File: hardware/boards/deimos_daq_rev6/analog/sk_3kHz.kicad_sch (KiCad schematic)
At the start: 9 parts, among them U17001 OPA196xDBV

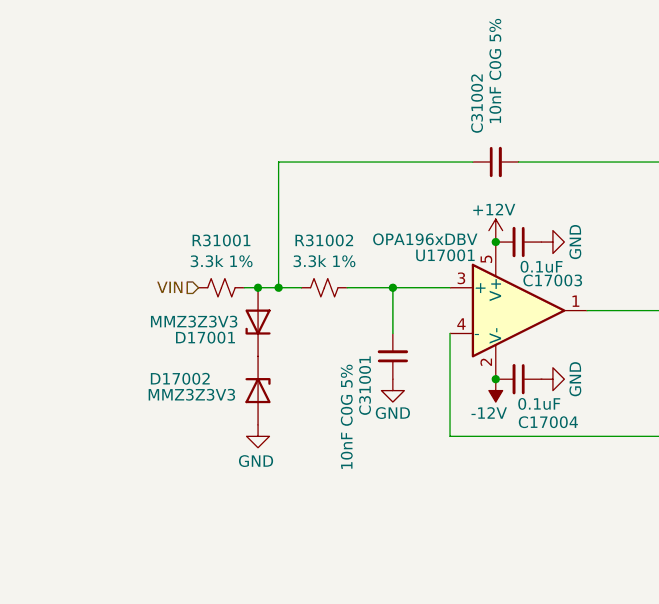
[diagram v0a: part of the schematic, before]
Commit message: move clamp diodes in schematic for filters. Add pulldown on ktype amp.
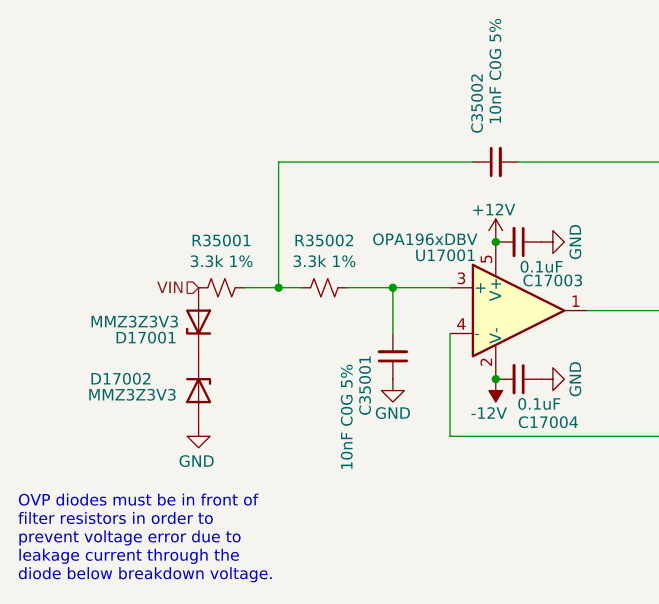
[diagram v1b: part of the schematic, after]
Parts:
- renumbered C31001 to C35001, C31002 to C35002, R31001 to R35001, R31002 to R35002
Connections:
- net VIN: now also D17001.2 (A)
- net at C35002.1, R35001.2, R35002.1: no longer D17001.2 (A)
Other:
- note added: "OVP diodes must be in front of filter resistors in order to prevent voltage error due to leakage current through the diode below breakdown voltage."
- moved on the sheet: D17001, D17002
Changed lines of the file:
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@@
-	)
-	(junction
-		(at 86.614 82.55)
-		(diameter 0)
-		(color 0 0 0 0)
 	)
 	(junction
@@
 	(wire
 		(pts
-			(xy 85.09 82.55) (xy 86.614 82.55)
+			(xy 85.09 82.55) (xy 88.9 82.55)
 		)
 		(stroke
@@
 	(wire
 		(pts
-			(xy 86.614 82.55) (xy 88.9 82.55)
+			(xy 107.95 99.06) (xy 133.35 99.06)
 		)
 		(stroke
@@
 	(wire
 		(pts
-			(xy 107.95 99.06) (xy 133.35 99.06)
+			(xy 101.6 82.55) (xy 107.95 82.55)
 		)
 		(stroke
@@
 	(wire
 		(pts
-			(xy 101.6 82.55) (xy 107.95 82.55)
+			(xy 88.9 68.58) (xy 88.9 82.55)
 		)
 		(stroke
@@
 	(wire
 		(pts
-			(xy 88.9 68.58) (xy 88.9 82.55)
+			(xy 110.49 68.58) (xy 88.9 68.58)
 		)
 		(stroke
@@
 	(wire
 		(pts
-			(xy 110.49 68.58) (xy 88.9 68.58)
+			(xy 133.35 99.06) (xy 133.35 85.09)
 		)
 		(stroke
@@
 		)
 	)
-	(wire
-		(pts
-			(xy 133.35 99.06) (xy 133.35 85.09)
-		)
-		(stroke
-			(width 0)
-			(type default)
+	(text "OVP diodes must be in front of\nfilter resistors in order to\nprevent voltage error due to\nleakage current through the\ndiode below breakdown voltage."
+		(exclude_from_sim no)
+		(at 59.944 110.49 0)
+		(effects
+			(font
+				(size 1.27 1.27)
+			)
+			(justify left)
 		)
 	)
@@
 		(on_board yes)
 		(dnp no)
-		(property "Reference" "C31001"
+		(property "Reference" "C35001"
 			(at 98.552 96.774 90)
 			(effects
@@
 	(symbol
 		(lib_id "Device:D_Zener")
-		(at 86.614 93.98 270)
+		(at 80.01 93.98 270)
 		(unit 1)
 		(exclude_from_sim no)
@@
 		(dnp no)
 		(property "Reference" "D17002"
-			(at 77.978 92.71 90)
+			(at 71.374 92.71 90)
 			(effects
 				(font
@@
 		)
 		(property "Value" "MMZ3Z3V3"
-			(at 79.248 94.488 90)
+			(at 72.644 94.488 90)
 			(effects
 				(font
@@
 		)
 		(property "Footprint" "Diode_SMD:D_SOD-323"
-			(at 86.614 93.98 0)
+			(at 80.01 93.98 0)
 			(effects
 				(font
@@
 		)
 		(property "Datasheet" "~"
-			(at 86.614 93.98 0)
+			(at 80.01 93.98 0)
 			(effects
 				(font
@@
 		)
 		(property "Description" ""
-			(at 86.614 93.98 0)
+			(at 80.01 93.98 0)
 			(effects
 				(font
@@
 		)
 		(property "LCSC" "C52056"
-			(at 86.614 93.98 0)
+			(at 80.01 93.98 0)
 			(effects
 				(font
@@
 	(symbol
 		(lib_id "Device:D_Zener")
-		(at 86.614 86.36 90)
+		(at 80.01 86.36 90)
 		(unit 1)
 		(exclude_from_sim no)
@@
 		(dnp no)
 		(property "Reference" "D17001"
-			(at 80.772 88.138 90)
+			(at 74.168 88.138 90)
 			(effects
 				(font
@@
 		)
 		(property "Value" "MMZ3Z3V3"
-			(at 79.502 86.36 90)
+			(at 72.898 86.36 90)
 			(effects
 				(font
@@
 		)
 		(property "Footprint" "Diode_SMD:D_SOD-323"
-			(at 86.614 86.36 0)
+			(at 80.01 86.36 0)
 			(effects
 				(font
@@
 		)
 		(property "Datasheet" "~"
-			(at 86.614 86.36 0)
+			(at 80.01 86.36 0)
 			(effects
 				(font
@@
 		)
 		(property "Description" ""
-			(at 86.614 86.36 0)
+			(at 80.01 86.36 0)
 			(effects
 				(font
@@
 		)
 		(property "LCSC" "C52056"
-			(at 86.614 86.36 0)
+			(at 80.01 86.36 0)
 			(effects
 				(font
@@
 	(symbol
 		(lib_id "power:GND")
-		(at 86.614 97.79 0)
+		(at 80.01 97.79 0)
 		(unit 1)
 		(exclude_from_sim no)
@@
 		(dnp no)
 		(property "Reference" "#PWR17002"
-			(at 86.614 104.14 0)
+			(at 80.01 104.14 0)
 			(effects
 				(font
@@
 		)
 		(property "Value" "GND"
-			(at 88.392 101.854 0)
+			(at 81.788 101.854 0)
 			(effects
 				(font
@@
 		)
 		(property "Footprint" ""
-			(at 86.614 97.79 0)
+			(at 80.01 97.79 0)
 			(effects
 				(font
@@
 		)
 		(property "Datasheet" ""
-			(at 86.614 97.79 0)
+			(at 80.01 97.79 0)
 			(effects
 				(font
@@
 		)
 		(property "Description" ""
-			(at 86.614 97.79 0)
+			(at 80.01 97.79 0)
 			(effects
 				(font
@@
 		(on_board yes)
 		(dnp no)
-		(property "Reference" "R31001"
+		(property "Reference" "R35001"
 			(at 82.55 77.343 90)
 			(effects
@@
 		(on_board yes)
 		(dnp no)
-		(property "Reference" "R31002"
+		(property "Reference" "R35002"
 			(at 93.98 77.343 90)
 			(effects
@@
 		(on_board yes)
 		(dnp no)
-		(property "Reference" "C31002"
+		(property "Reference" "C35002"
 			(at 110.998 58.674 0)
 			(effects
@@
 		(on_board yes)
 		(dnp no)
-		(property "Reference" "#PWR195"
+		(property "Reference" "#PWR205"
 			(at 101.6 99.06 0)
 			(effects

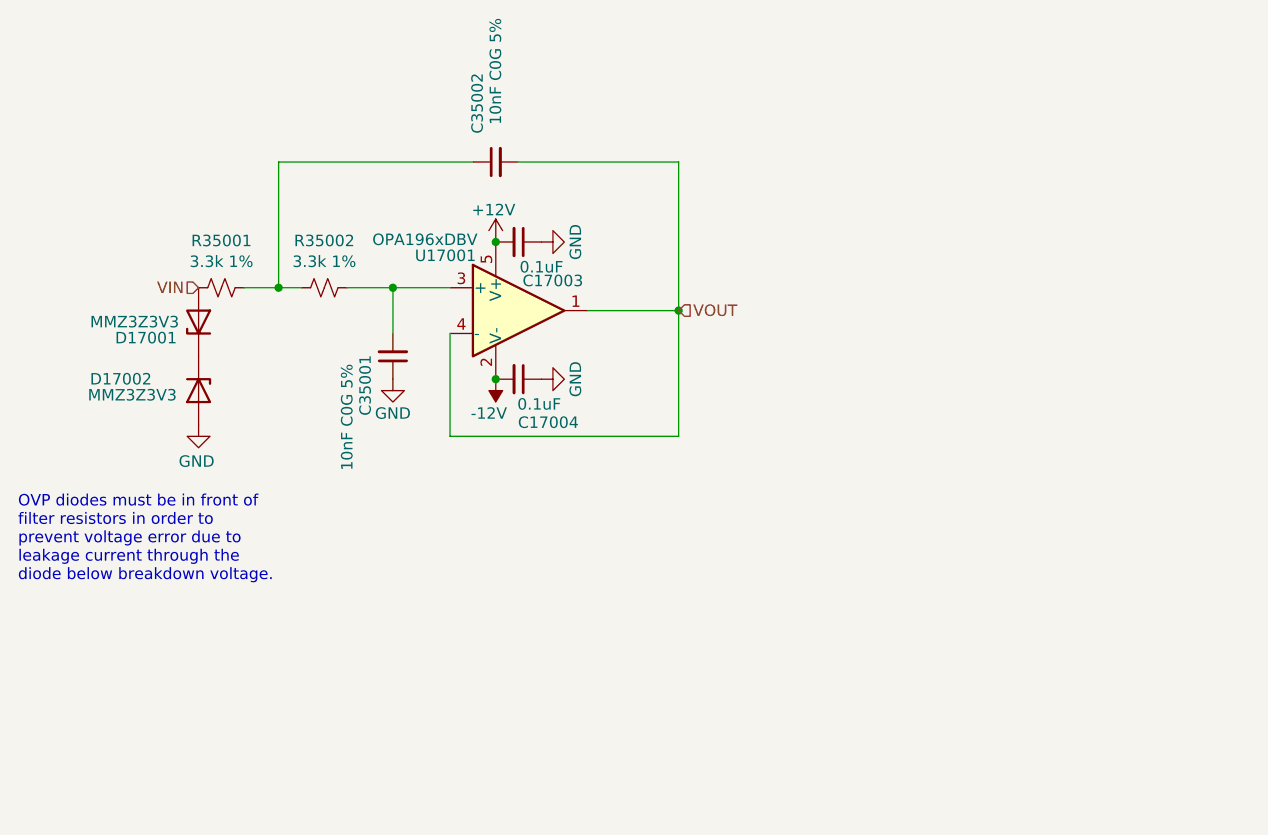
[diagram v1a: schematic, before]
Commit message: move ovp diodes behind filter amps. wip to implement 5V LDO.
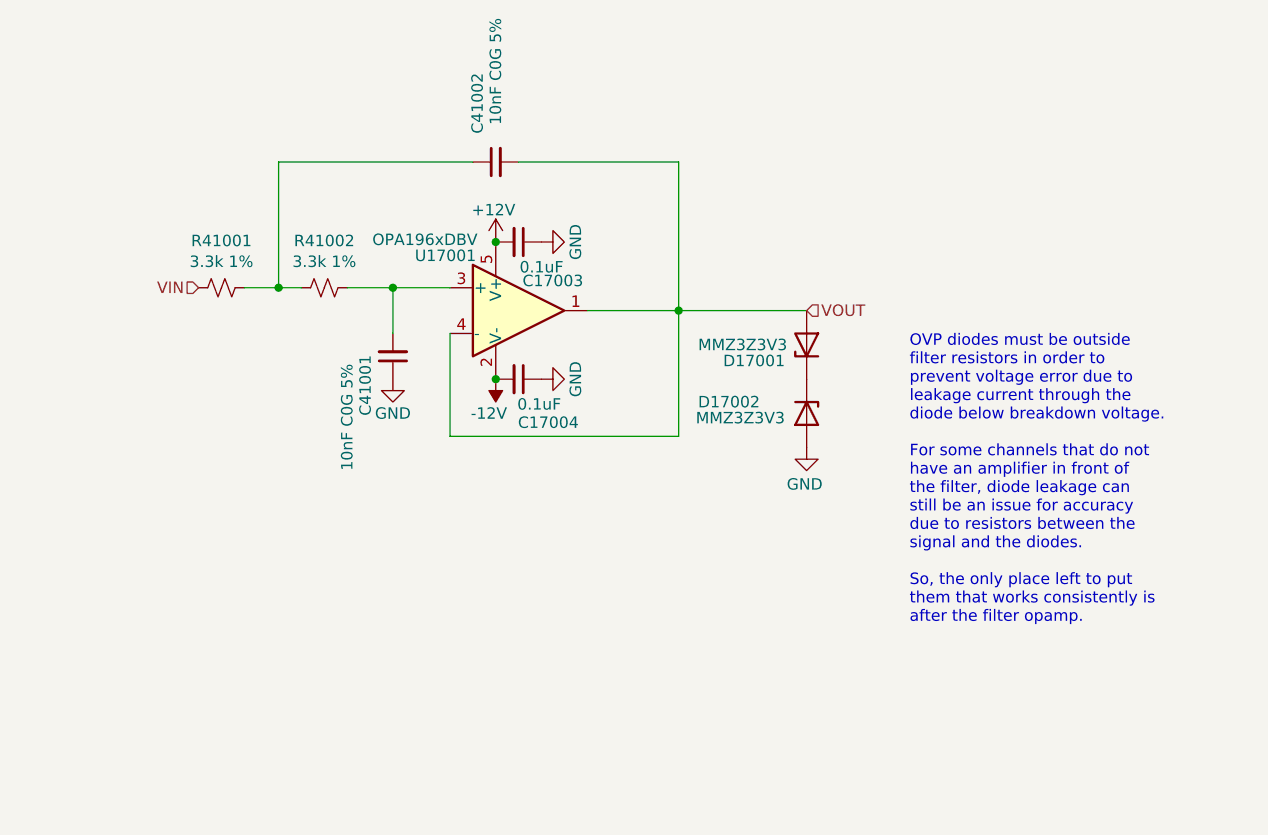
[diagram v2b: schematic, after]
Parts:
- renumbered C35001 to C41001, C35002 to C41002, R35001 to R41001, R35002 to R41002
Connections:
- net VIN: no longer D17001.2 (A)
- net VOUT: now also D17001.2 (A)
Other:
- note added: "OVP diodes must be outside filter resistors in order to prevent voltage error due to leakage current through the diode below breakdown voltage. For some channels that do not have an amplifier in front of the filter, diode leakage can still be an issue for accuracy due to resistors between the signal and the diodes. So, the only place left to put them that works consistently is after the filter op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"
- note removed: "OVP diodes must be in front of filter resistors in order to prevent voltage error due to leakage current through the diode below breakdown voltage."
- moved on the sheet: D17001, D17002
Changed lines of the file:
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@@
+	(wire
+		(pts
+			(xy 133.35 85.09) (xy 147.574 85.09)
+		)
+		(stroke
+			(width 0)
+			(type default)
+		)
+	)
 	(wire
 		(pts
@@
 		)
 	)
-	(text "OVP diodes must be in front of\nfilter resistors in order to\nprevent voltage error due to\nleakage current through the\ndiode below breakdown voltage."
+	(text "OVP diodes must be outside\nfilter resistors in order to\nprevent voltage error due to\nleakage current through the\ndiode below breakdown voltage.\n\nFor some channels that do not\nhave an amplifier in front of\nthe filter, diode leakage can\nstill be an issue for accuracy\ndue to resistors between the\nsignal and the diodes.\n\nSo, the only place left to put\nthem that works consistently is\nafter the filter opamp."
 		(exclude_from_sim no)
-		(at 59.944 110.49 0)
+		(at 159.004 103.886 0)
 		(effects
 			(font
@@
 	(hierarchical_label "VOUT"
 		(shape input)
-		(at 133.35 85.09 0)
+		(at 147.574 85.09 0)
 		(effects
 			(font
@@
 		(on_board yes)
 		(dnp no)
-		(property "Reference" "C35001"
+		(property "Reference" "C41001"
 			(at 98.552 96.774 90)
 			(effects
@@
 	(symbol
 		(lib_id "Device:D_Zener")
-		(at 80.01 93.98 270)
+		(at 147.574 96.52 270)
 		(unit 1)
 		(exclude_from_sim no)
@@
 		(dnp no)
 		(property "Reference" "D17002"
-			(at 71.374 92.71 90)
+			(at 138.938 95.25 90)
 			(effects
 				(font
@@
 		)
 		(property "Value" "MMZ3Z3V3"
-			(at 72.644 94.488 90)
+			(at 140.208 97.028 90)
 			(effects
 				(font
@@
 		)
 		(property "Footprint" "Diode_SMD:D_SOD-323"
-			(at 80.01 93.98 0)
+			(at 147.574 96.52 0)
 			(effects
 				(font
@@
 		)
 		(property "Datasheet" "~"
-			(at 80.01 93.98 0)
+			(at 147.574 96.52 0)
 			(effects
 				(font
@@
 		)
 		(property "Description" ""
-			(at 80.01 93.98 0)
+			(at 147.574 96.52 0)
 			(effects
 				(font
@@
 		)
 		(property "LCSC" "C52056"
-			(at 80.01 93.98 0)
+			(at 147.574 96.52 0)
 			(effects
 				(font
@@
 	(symbol
 		(lib_id "Device:D_Zener")
-		(at 80.01 86.36 90)
+		(at 147.574 88.9 90)
 		(unit 1)
 		(exclude_from_sim no)
@@
 		(dnp no)
 		(property "Reference" "D17001"
-			(at 74.168 88.138 90)
+			(at 141.732 90.678 90)
 			(effects
 				(font
@@
 		)
 		(property "Value" "MMZ3Z3V3"
-			(at 72.898 86.36 90)
+			(at 140.462 88.9 90)
 			(effects
 				(font
@@
 		)
 		(property "Footprint" "Diode_SMD:D_SOD-323"
-			(at 80.01 86.36 0)
+			(at 147.574 88.9 0)
 			(effects
 				(font
@@
 		)
 		(property "Datasheet" "~"
-			(at 80.01 86.36 0)
+			(at 147.574 88.9 0)
 			(effects
 				(font
@@
 		)
 		(property "Description" ""
-			(at 80.01 86.36 0)
+			(at 147.574 88.9 0)
 			(effects
 				(font
@@
 		)
 		(property "LCSC" "C52056"
-			(at 80.01 86.36 0)
+			(at 147.574 88.9 0)
 			(effects
 				(font
@@
 	(symbol
 		(lib_id "power:GND")
-		(at 80.01 97.79 0)
+		(at 147.574 100.33 0)
 		(unit 1)
 		(exclude_from_sim no)
@@
 		(dnp no)
 		(property "Reference" "#PWR17002"
-			(at 80.01 104.14 0)
+			(at 147.574 106.68 0)
 			(effects
 				(font
@@
 		)
 		(property "Value" "GND"
-			(at 81.788 101.854 0)
+			(at 149.352 104.394 0)
 			(effects
 				(font
@@
 		)
 		(property "Footprint" ""
-			(at 80.01 97.79 0)
+			(at 147.574 100.33 0)
 			(effects
 				(font
@@
 		)
 		(property "Datasheet" ""
-			(at 80.01 97.79 0)
+			(at 147.574 100.33 0)
 			(effects
 				(font
@@
 		)
 		(property "Description" ""
-			(at 80.01 97.79 0)
+			(at 147.574 100.33 0)
 			(effects
 				(font
@@
 		(on_board yes)
 		(dnp no)
-		(property "Reference" "R35001"
+		(property "Reference" "R41001"
 			(at 82.55 77.343 90)
 			(effects
@@
 		(on_board yes)
 		(dnp no)
-		(property "Reference" "R35002"
+		(property "Reference" "R41002"
 			(at 93.98 77.343 90)
 			(effects
@@
 		(on_board yes)
 		(dnp no)
-		(property "Reference" "C35002"
+		(property "Reference" "C41002"
 			(at 110.998 58.674 0)
 			(effects
@@
 		(on_board yes)
 		(dnp no)
-		(property "Reference" "#PWR205"
+		(property "Reference" "#PWR232"
 			(at 101.6 99.06 0)
 			(effects

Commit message: figure out divider for 5V LDO. update input filter for resistance amp to cause less error.
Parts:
- renumbered C41001 to C31001, C41002 to C31002, R41001 to R31001, R41002 to R31002
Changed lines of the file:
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@@
 		(on_board yes)
 		(dnp no)
-		(property "Reference" "C41001"
+		(property "Reference" "C31001"
 			(at 98.552 96.774 90)
 			(effects
@@
 		(on_board yes)
 		(dnp no)
-		(property "Reference" "R41001"
+		(property "Reference" "R31001"
 			(at 82.55 77.343 90)
 			(effects
@@
 		(on_board yes)
 		(dnp no)
-		(property "Reference" "R41002"
+		(property "Reference" "R31002"
 			(at 93.98 77.343 90)
 			(effects
@@
 		(on_board yes)
 		(dnp no)
-		(property "Reference" "C41002"
+		(property "Reference" "C31002"
 			(at 110.998 58.674 0)
 			(effects
@@
 		(on_board yes)
 		(dnp no)
-		(property "Reference" "#PWR232"
+		(property "Reference" "#PWR195"
 			(at 101.6 99.06 0)
 			(effects

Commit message: label 5v ldo
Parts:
- renumbered C31001 to C41001, C31002 to C41002, R31001 to R41001, R31002 to R41002
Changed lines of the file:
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@@
 		(on_board yes)
 		(dnp no)
-		(property "Reference" "C31001"
+		(property "Reference" "C41001"
 			(at 98.552 96.774 90)
 			(effects
@@
 		(on_board yes)
 		(dnp no)
-		(property "Reference" "R31001"
+		(property "Reference" "R41001"
 			(at 82.55 77.343 90)
 			(effects
@@
 		(on_board yes)
 		(dnp no)
-		(property "Reference" "R31002"
+		(property "Reference" "R41002"
 			(at 93.98 77.343 90)
 			(effects
@@
 		(on_board yes)
 		(dnp no)
-		(property "Reference" "C31002"
+		(property "Reference" "C41002"
 			(at 110.998 58.674 0)
 			(effects
@@
 		(on_board yes)
 		(dnp no)
-		(property "Reference" "#PWR195"
+		(property "Reference" "#PWR232"
 			(at 101.6 99.06 0)
 			(effects

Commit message: run rtd amp current sinks on 5V supply
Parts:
- renumbered C41001 to C35001, C41002 to C35002, R41001 to R35001, R41002 to R35002
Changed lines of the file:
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@@
 		(on_board yes)
 		(dnp no)
-		(property "Reference" "C41001"
+		(property "Reference" "C35001"
 			(at 98.552 96.774 90)
 			(effects
@@
 		(on_board yes)
 		(dnp no)
-		(property "Reference" "R41001"
+		(property "Reference" "R35001"
 			(at 82.55 77.343 90)
 			(effects
@@
 		(on_board yes)
 		(dnp no)
-		(property "Reference" "R41002"
+		(property "Reference" "R35002"
 			(at 93.98 77.343 90)
 			(effects
@@
 		(on_board yes)
 		(dnp no)
-		(property "Reference" "C41002"
+		(property "Reference" "C35002"
 			(at 110.998 58.674 0)
 			(effects
@@
 		(on_board yes)
 		(dnp no)
-		(property "Reference" "#PWR232"
+		(property "Reference" "#PWR205"
 			(at 101.6 99.06 0)
 			(effects
